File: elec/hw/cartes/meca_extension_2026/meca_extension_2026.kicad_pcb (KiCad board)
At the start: 2 copper layers, 178.8 x 200.5 mm, 175 parts, among them J1 2-1445055-3, J10 22053051, J11 B2B-XH-A, J12 22272021, J13 22053051, J14 22272031, J15 22272031, J16 5264-3P, J17 5267-3P, J18 5267-3P, J19 5267-3P, J2 B2B-XH-A, J20 5267-3P, J24 22053031, J25 22053031, J26 22053051, J27 22053041, J28 22053031, J29 22053031, J3 22272021, J4 22053051, J5 B2B-XH-A, J6 22272021, J7 22053051, J8 B2B-XH-A, J9 22272021, Q1 SI2310, Q10 SI2310, Q11 SI2310, Q12 2N7002, Q19 BSS84, Q2 SI2310, Q20 2N7002, Q3 2N7002, Q4 SI2310, Q5 SI2310, Q6 2N7002, Q7 SI2310, Q8 SI2310, Q9 2N7002, U1 TCA9548APWR, U11 LV14340DDAR, U2 PCA9535PW, U3 TLA2528IRTER, U4 TLV9061IDBVR, U5 TLV9061IDBVR, U6 TLV9061IDBVR, U7 TLV9061IDBVR, U8 74HCT238PW

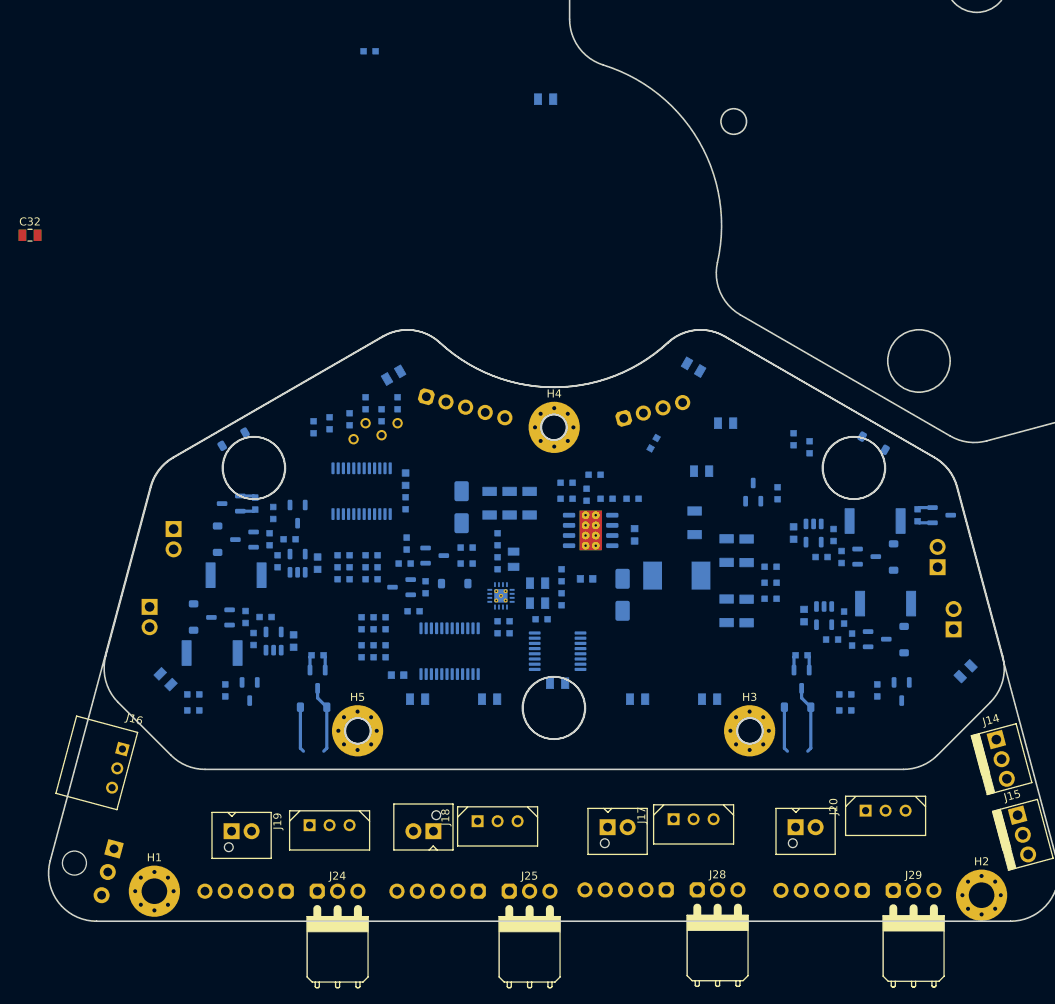
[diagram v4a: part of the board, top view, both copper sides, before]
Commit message: meca_extension : more component placement
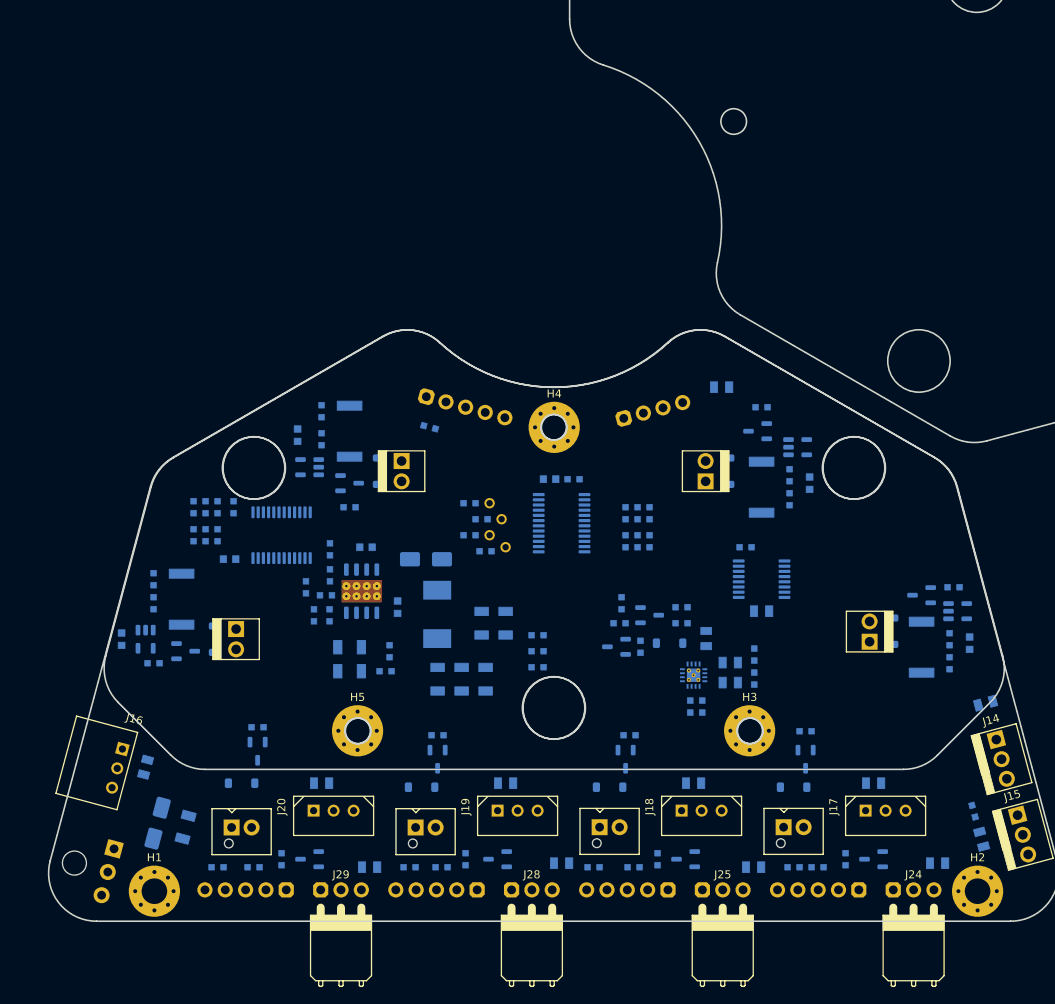
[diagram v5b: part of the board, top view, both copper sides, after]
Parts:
- C32: moved to B.Cu
- J12, J3, J6, J9: moved to F.Cu
- moved R42 72.5 mm to (107.5, 124.0), turned to 0 degrees
- moved J24 72.0 mm to (170.5, 126.8)
- moved J29 71.6 mm to (98.9, 126.8)
- moved D5 71.0 mm to (109.0, 114.0), turned to 0 degrees
- moved Q7 70.0 mm to (111.0, 110.5), turned to -90 degrees
- moved R44 69.3 mm to (111.5, 124.0), turned to 180 degrees
- moved J20 69.0 mm to (98.0, 116.9)
- moved C27 68.2 mm to (173.5, 123.5), turned to 0 degrees
- moved C32 68.1 mm to (74.5, 111.5), turned to 75 degrees
- moved R36 68.0 mm to (135.5, 124.0), turned to 180 degrees
- moved J9 67.9 mm to (106.5, 74.5)
- moved J6 67.0 mm to (144.5, 74.5)
- moved R41 66.6 mm to (100.0, 69.5), turned to 90 degrees
- moved R33 66.6 mm to (151.5, 76.5), turned to -90 degrees
- moved R39 66.0 mm to (111.0, 107.5), turned to 0 degrees
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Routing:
- net +BATT: track 11.3 -> 0.00 mm
- net Net-(D7-A): track 8.50 -> 0.00 mm
- net Net-(D1-A): track 8.50 -> 0.00 mm
- net GND: track 7.78 -> 0.00 mm
- net /solenoid_valve_cmd_2_3v3: track 1.95 -> 0.00 mm
- net /solenoid_valve_cmd_3_3v3: track 1.95 -> 0.00 mm
- net /solenoid_valve_cmd_1_3v3: track 1.95 -> 0.00 mm
- net /solenoid_valve_cmd_0_3v3: track 1.95 -> 0.00 mm

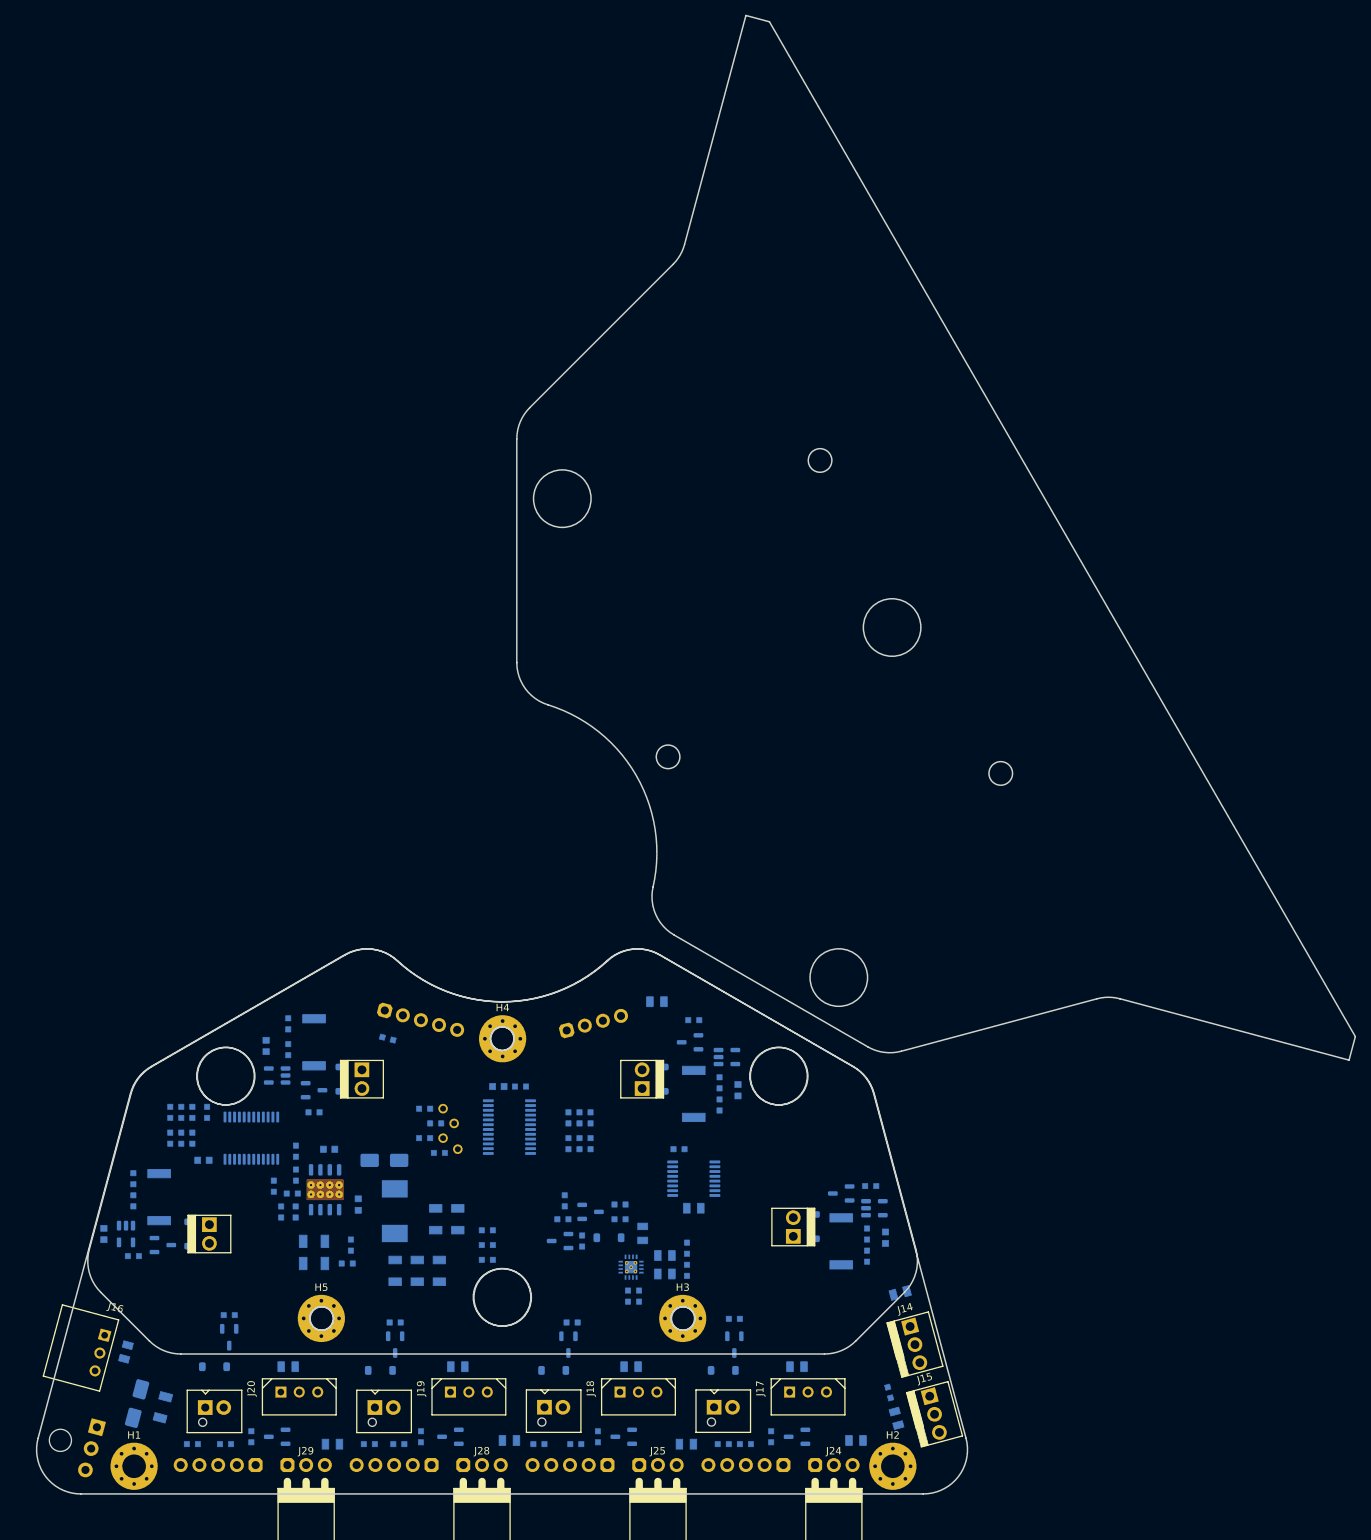
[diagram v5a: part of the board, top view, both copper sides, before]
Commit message: meca_extension: implant modified and integrated into CAD
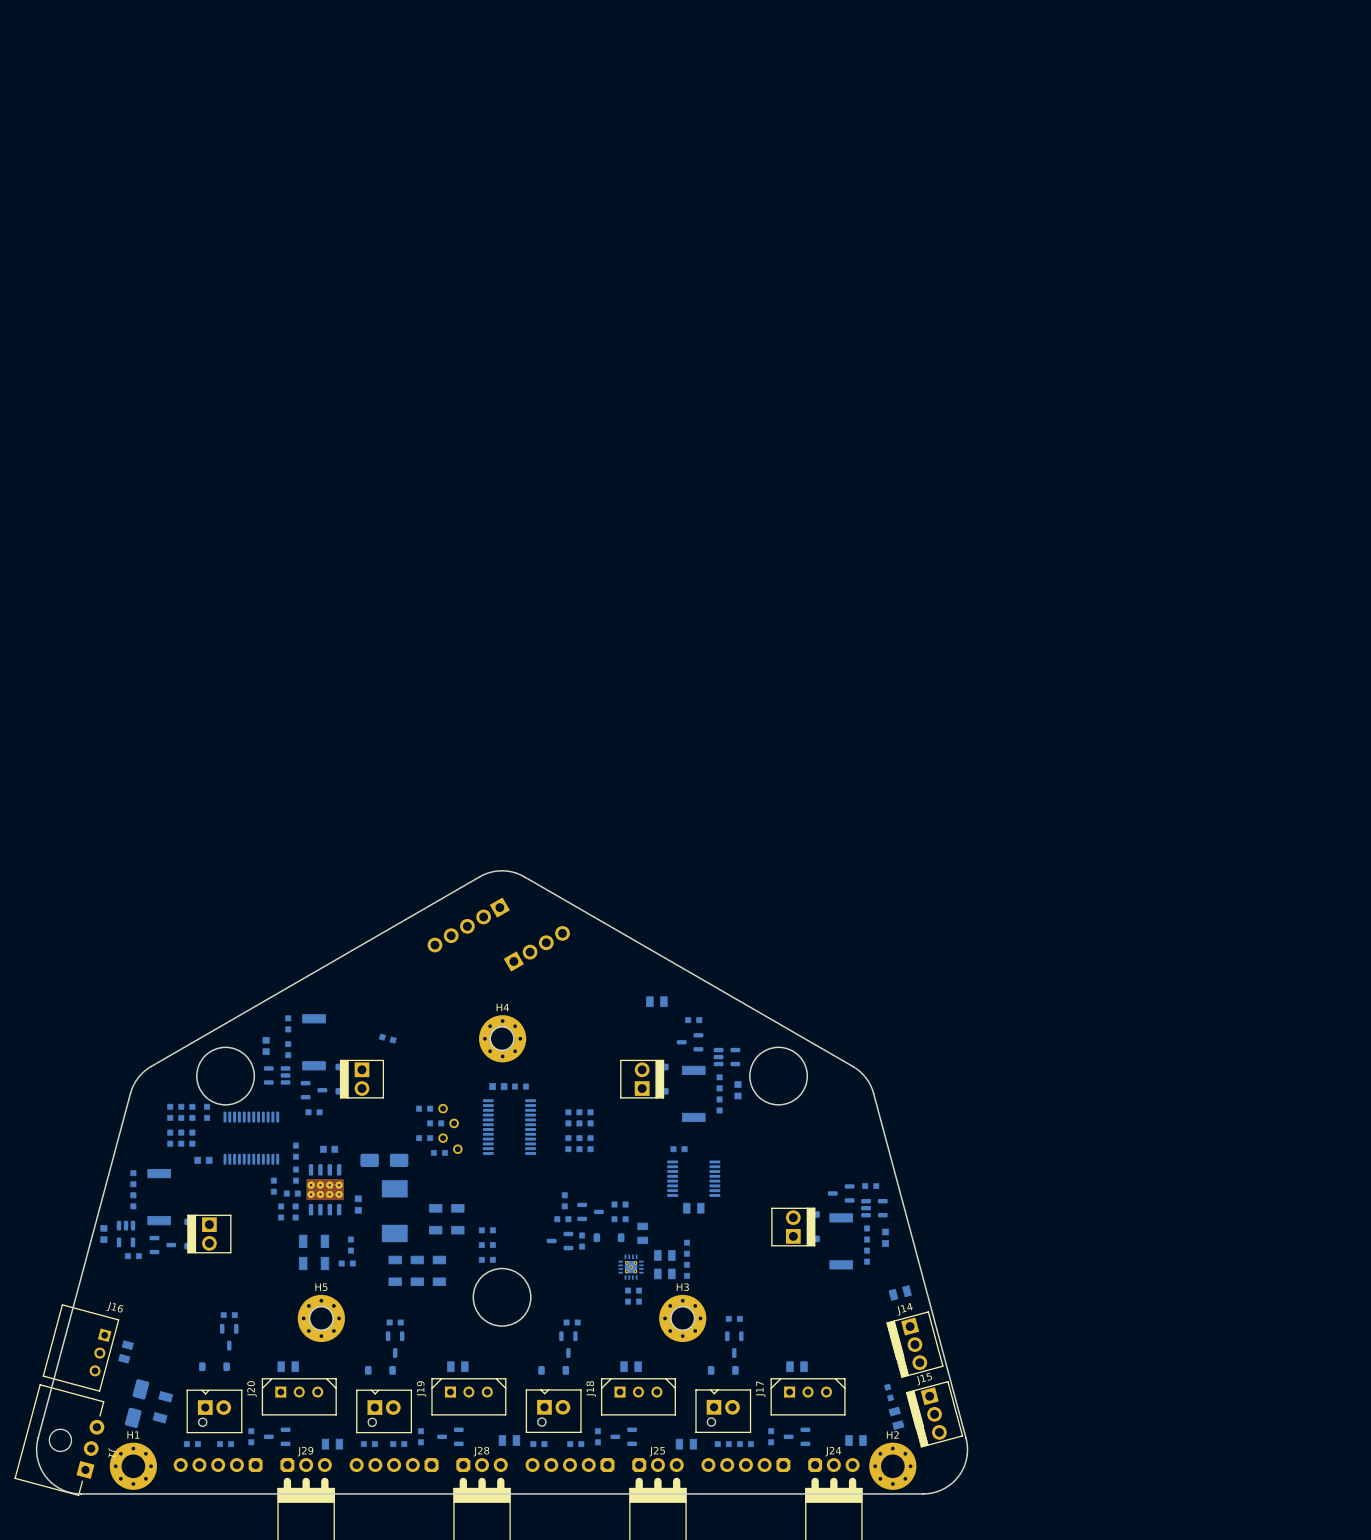
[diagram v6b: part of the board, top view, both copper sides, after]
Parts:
- J1: moved to F.Cu
- J26: footprint cocotter_connectors:22053051 -> cocotter_connectors:22272051
- J27: footprint cocotter_connectors:22053041 -> cocotter_connectors:22272041
- moved J26 14.2 mm to (120.8, 53.8), turned to 120 degrees
- moved J27 12.7 mm to (130.4, 56.6), turned to -60 degrees
- moved H1 0.10 mm to (75.5, 127.0)
- turned J1 to -105 degrees
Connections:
- J27 pad 1: GND -> /scl_3v3
- J27 pad 2: /scl_3v3 -> /sda_3v3
- J27 pad 3: /sda_3v3 -> +3.3V
- J27 pad 4: +3.3V -> unconnected-(J27-Pad4)
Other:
- board size 178.8 x 200.5 mm -> 126.2 x 84.5 mm

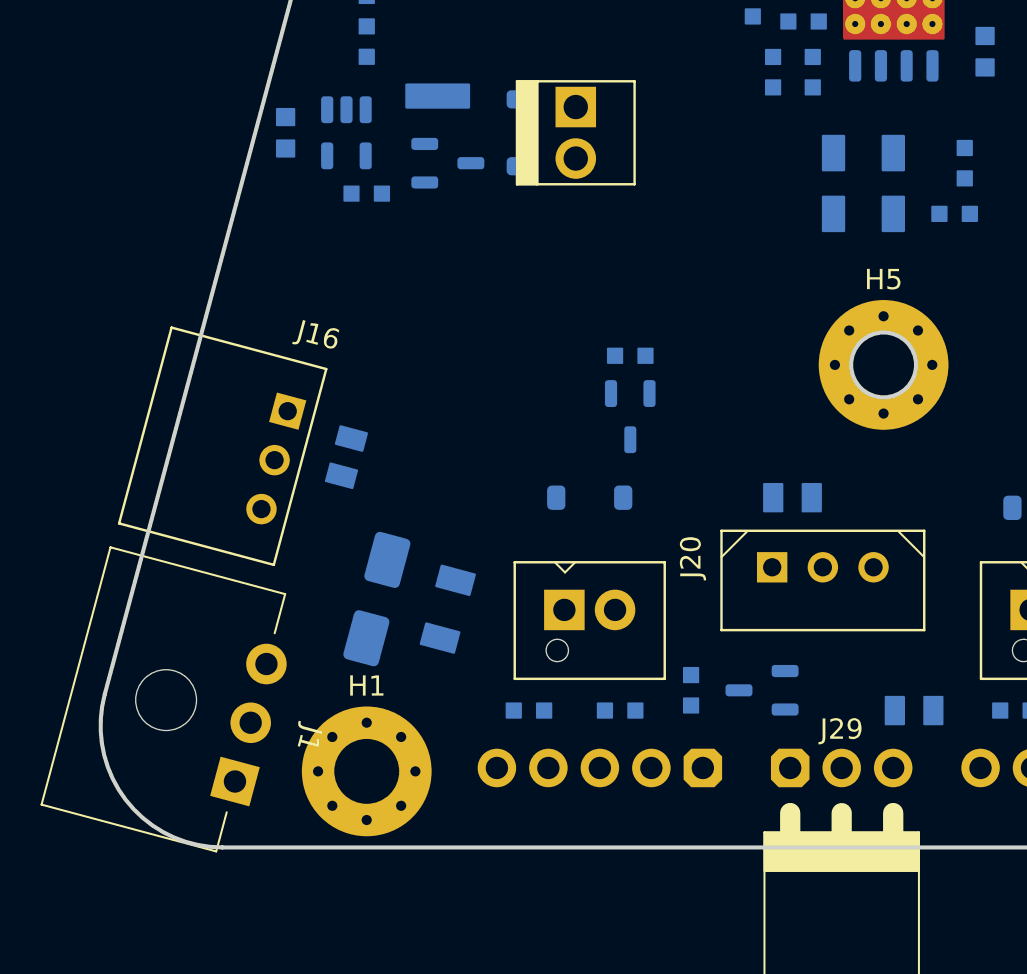
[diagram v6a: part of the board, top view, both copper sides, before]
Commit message: meca_extension : battery connector changed
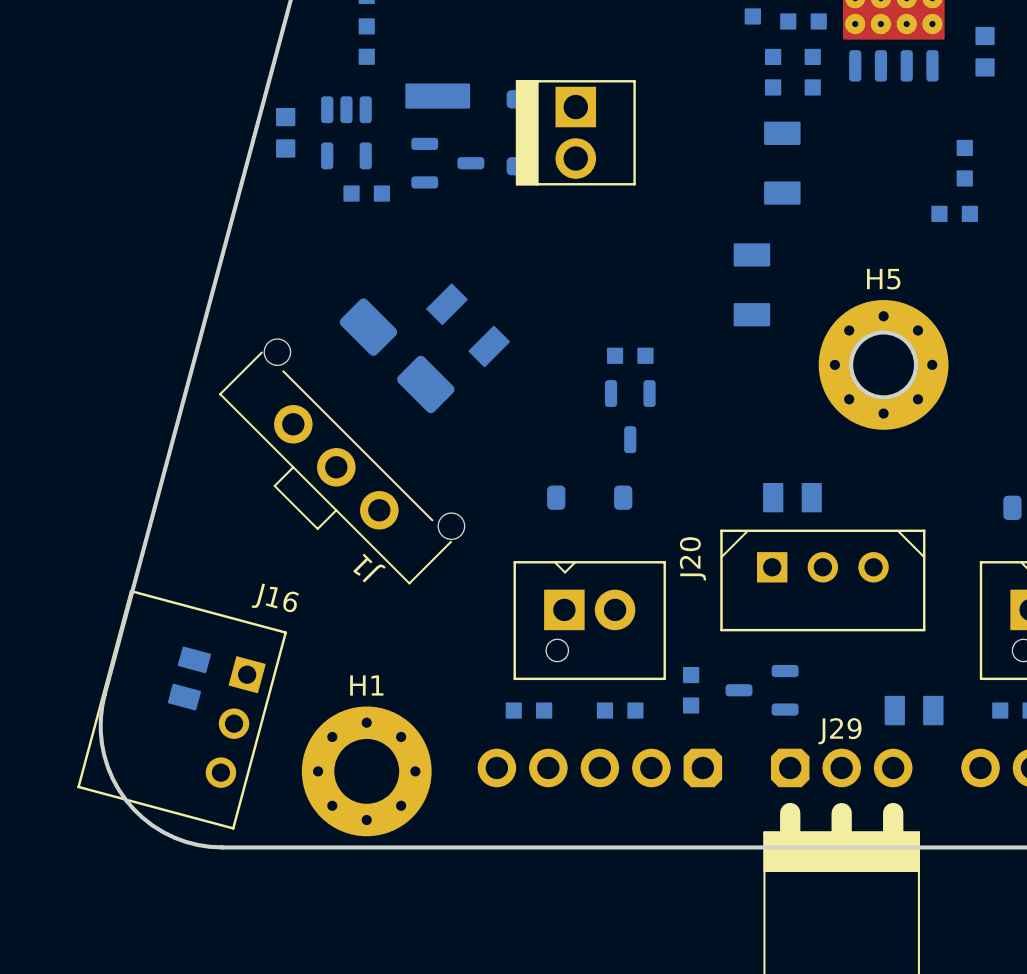
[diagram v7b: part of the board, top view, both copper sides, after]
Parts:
- J1: value 2-1445055-3 -> 2-1445051-3; footprint cocotter_connectors:2-1445055-3 -> cocotter_connectors:2-1445051-3
- moved C28 14.0 mm to (80.5, 105.0), turned to 135 degrees
- moved C32 13.4 mm to (66.8, 122.4)
- moved J1 13.3 mm to (74.0, 112.0), turned to 135 degrees
- moved J16 13.2 mm to (69.0, 124.6)
- moved D15 12.0 mm to (77.0, 106.5), turned to 135 degrees
- moved C21 6.52 mm to (94.5, 103.0), turned to -90 degrees
- moved C13 4.03 mm to (96.0, 97.0), turned to 90 degrees

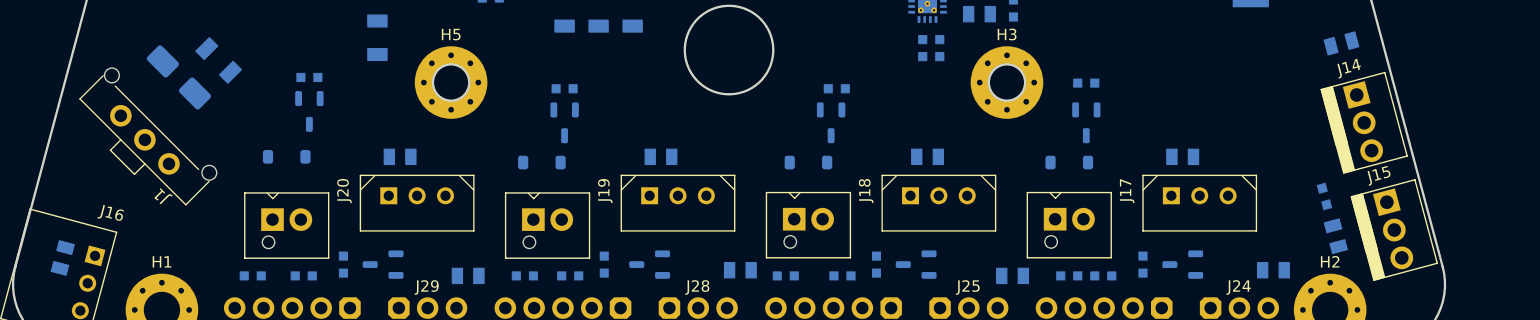
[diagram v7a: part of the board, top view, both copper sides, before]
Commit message: meca_extension : led added and J1 moved
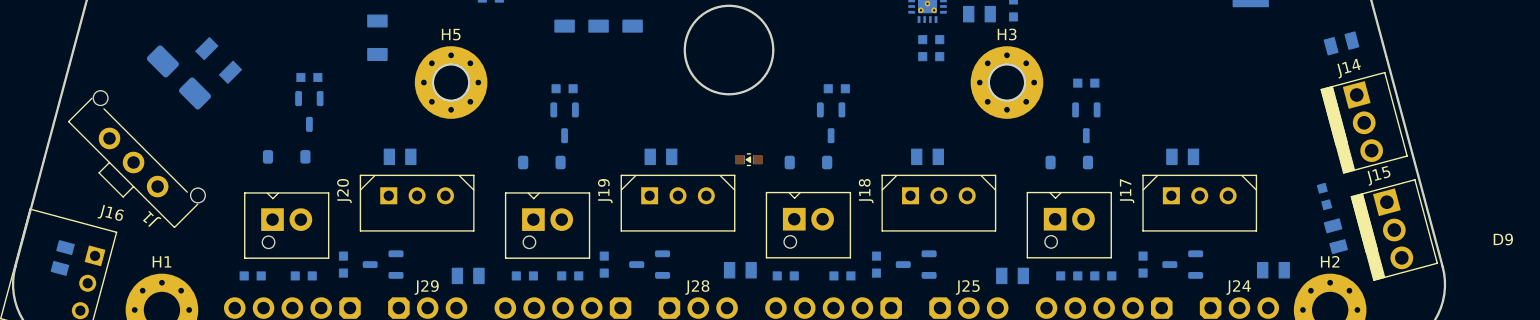
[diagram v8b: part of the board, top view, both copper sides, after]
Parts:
- added D9: yellow, 0603, cocotter_diodes:LED_0603_1608Metric, F.Cu at (127.2, 113.8)
- added R57: 1k 1%, cocotter_resistor:r0603_reflow, B.Cu at (127.2, 113.8)
- moved J1 2.24 mm to (73.0, 114.0)
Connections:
- U2 pad 11: unconnected-(U2-IO0_7-Pad11) -> Net-(U2-IO0_7)
